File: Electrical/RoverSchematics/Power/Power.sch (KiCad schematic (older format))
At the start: 4 parts

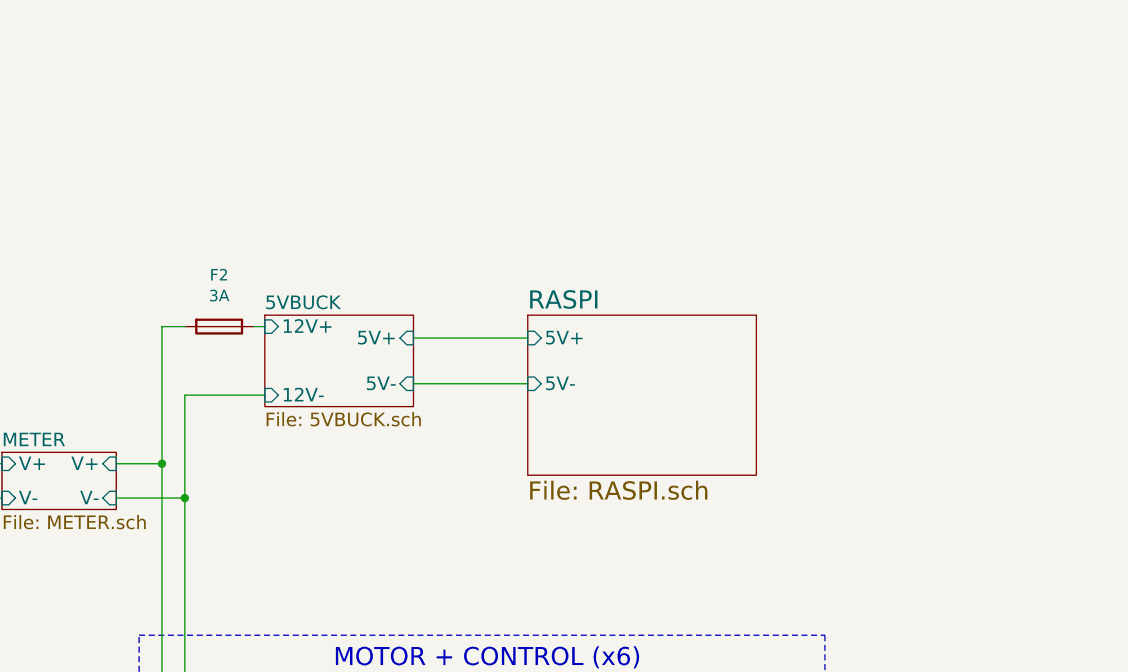
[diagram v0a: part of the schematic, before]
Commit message: Added PWM HAT and Servos to Block Diagram
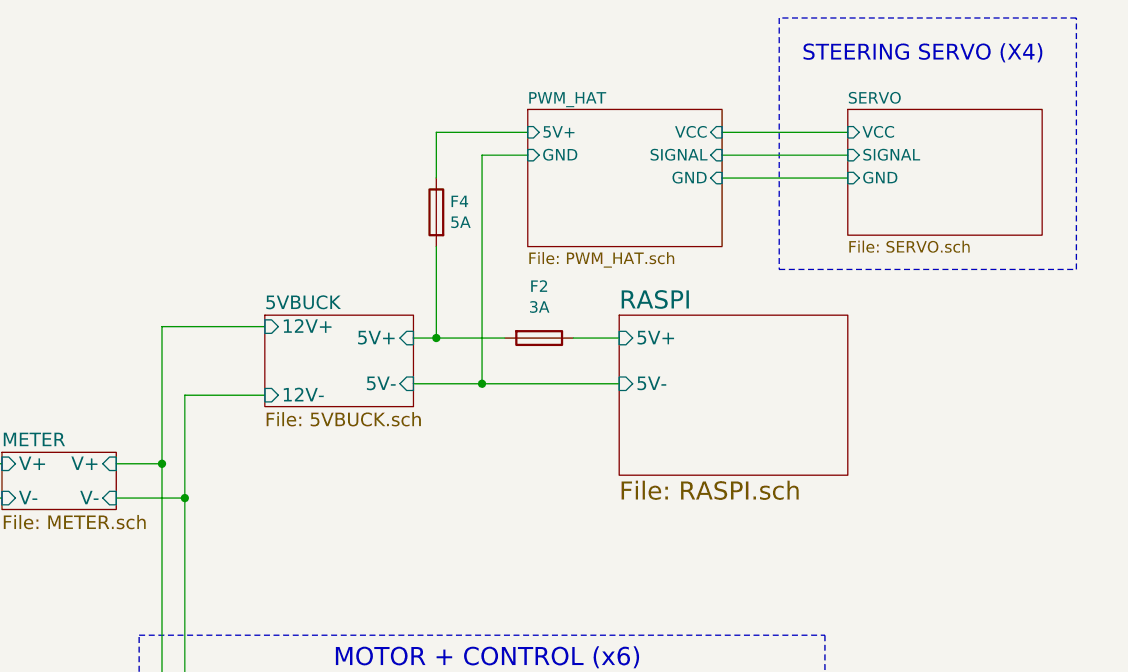
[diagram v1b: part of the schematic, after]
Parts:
- added F4: 5A, symbol Device:Fuse
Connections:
- net 5VBUCK/12V+: now also F3.2; no longer F2.1
- net 5VBUCK/5V+: now also F2.2, F4.2
- removed net METER/V+: F2.2, F3.2
- new net PWM_HAT/5V+: F4.1
- new net RASPI/5V+: F2.1
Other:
- note added: "STEERING SERVO (X4)"
- moved on the sheet: F2
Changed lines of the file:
@@
 EESchema Schematic File Version 4
+LIBS:Power-cache
 EELAYER 26 0
 EELAYER END
 $Descr A4 11693 8268
 encoding utf-8
-Sheet 1 8
+Sheet 1 10
 Title "MINIROVER POWER DIAGRAM"
 Date "2018-10-21"
@@
 L Device:Fuse F2
 U 1 1 5BD0A919
-P 5950 2550
-F 0 "F2" V 5725 2550 50  0000 C CNN
-F 1 "3A" V 5816 2550 50  0000 C CNN
-F 2 "" H 6000 2350 50  0001 L CNN
-F 3 "~" H 5950 2550 50  0001 C CNN
-	1    5950 2550
+P 7350 2600
+F 0 "F2" V 7125 2600 50  0000 C CNN
+F 1 "3A" V 7216 2600 50  0000 C CNN
+F 2 "" H 7400 2400 50  0001 L CNN
+F 3 "~" H 7350 2600 50  0001 C CNN
+	1    7350 2600
 	0    1    1    0
 $EndComp
-Wire Wire Line
-	5700 2550 5800 2550
-Wire Wire Line
-	6100 2550 6150 2550
 Wire Wire Line
 	5800 2850 6150 2850
@@
 	5800 4600 6300 4600
 $Sheet
-S 7300 2500 1000 700
+S 7700 2500 1000 700
 U 5BD0F6A9
 F0 "RASPI" 79
 F1 "RASPI.sch" 79
-F2 "5V+" I L 7300 2600 59
-F3 "5V-" I L 7300 2800 59
-$EndSheet
-Wire Wire Line
-	7300 2600 6800 2600
-Wire Wire Line
-	7300 2800 6800 2800
+F2 "5V+" I L 7700 2600 59
+F3 "5V-" I L 7700 2800 59
+$EndSheet
+$Sheet
+S 7300 1600 850  600
+U 5BDB4C8F
+F0 "PWM_HAT" 50
+F1 "PWM_HAT.sch" 50
+F2 "5V+" I L 7300 1700 50
+F3 "GND" I L 7300 1800 50
+F4 "VCC" I R 8150 1700 50
+F5 "SIGNAL" I R 8150 1800 50
+F6 "GND" I R 8150 1900 50
+$EndSheet
+Wire Wire Line
+	7300 1800 7100 1800
+Wire Wire Line
+	7100 1800 7100 2800
+Wire Wire Line
+	7100 2800 6800 2800
+$Sheet
+S 8700 1600 850  550
+U 5BDB5877
+F0 "SERVO" 50
+F1 "SERVO.sch" 50
+F2 "VCC" I L 8700 1700 50
+F3 "SIGNAL" I L 8700 1800 50
+F4 "GND" I L 8700 1900 50
+$EndSheet
+Wire Wire Line
+	8150 1700 8700 1700
+Wire Wire Line
+	8150 1800 8700 1800
+Wire Wire Line
+	8700 1900 8150 1900
+Wire Notes Line
+	8400 1200 8400 2300
+Wire Notes Line
+	8400 2300 9700 2300
+Wire Notes Line
+	9700 2300 9700 1200
+Wire Notes Line
+	9700 1200 8400 1200
+Text Notes 8500 1400 0    69   ~ 0
+STEERING SERVO (X4)
+Wire Wire Line
+	7100 2800 7700 2800
+Connection ~ 7100 2800
+Wire Wire Line
+	5700 2550 6150 2550
+Wire Wire Line
+	7500 2600 7700 2600
+Wire Wire Line
+	6800 2600 6900 2600
+$Comp
+L Device:Fuse F4
+U 1 1 5BDBADD3
+P 6900 2050
+F 0 "F4" H 6840 2096 50  0000 R CNN
+F 1 "5A" H 6840 2005 50  0000 R CNN
+F 2 "" V 6830 2050 50  0001 C CNN
+F 3 "~" H 6900 2050 50  0001 C CNN
+	1    6900 2050
+	-1   0    0    -1
+$EndComp
+Wire Wire Line
+	6900 1900 6900 1700
+Wire Wire Line
+	6900 2200 6900 2600
+Connection ~ 6900 2600
+Wire Wire Line
+	6900 2600 7200 2600
+Wire Wire Line
+	6900 1700 7300 1700
 $EndSCHEMATC

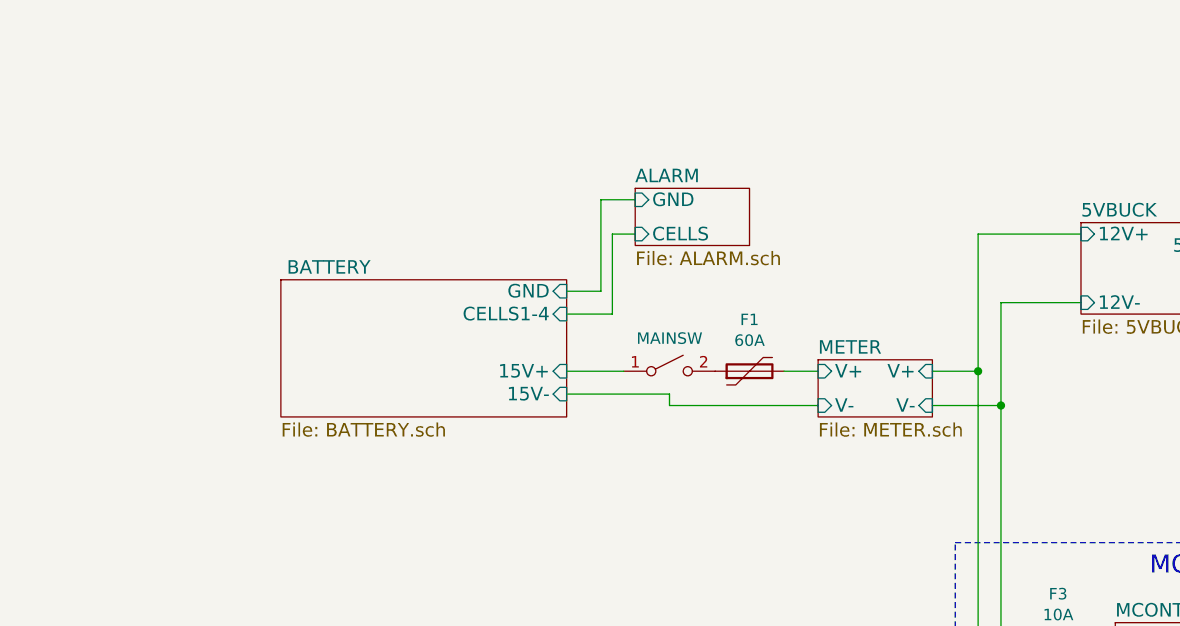
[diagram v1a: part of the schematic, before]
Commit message: Actually fixed drivetrain this time, various small changes
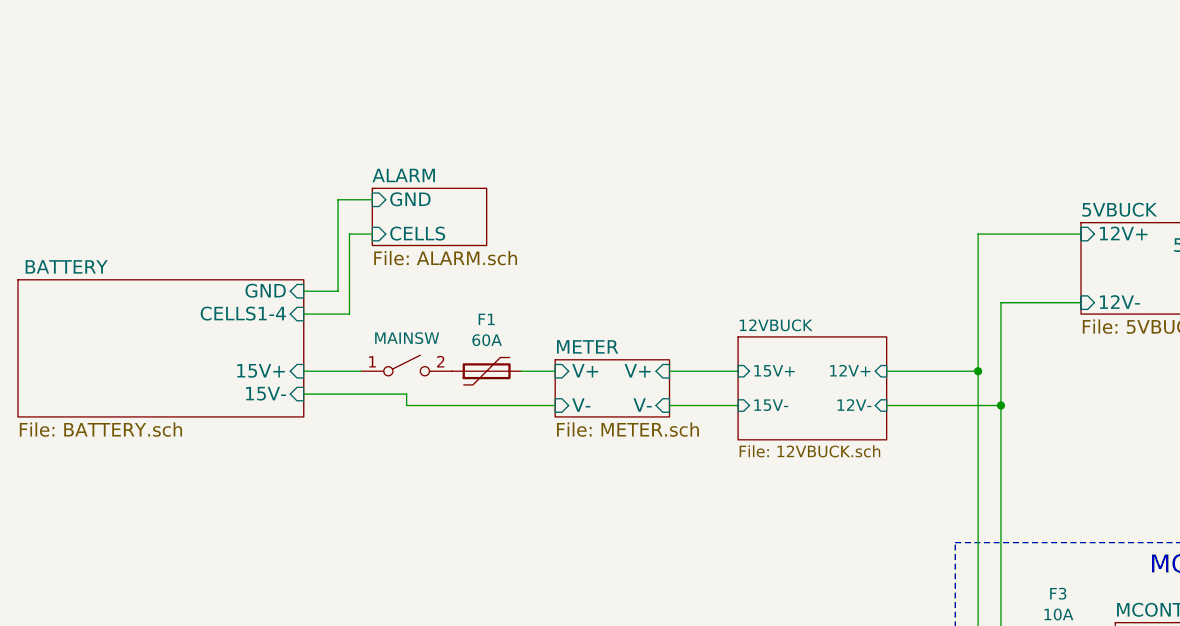
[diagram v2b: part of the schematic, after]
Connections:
- net 5VBUCK/12V+ renamed 12VBUCK/12V+
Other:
- moved on the sheet: F1, MAINSW
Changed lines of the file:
@@
 EESchema Schematic File Version 4
 LIBS:Power-cache
-EELAYER 26 0
+EELAYER 29 0
 EELAYER END
 $Descr A4 11693 8268
@@
 $EndDescr
 $Sheet
-S 2650 2750 1250 600
+S 1500 2750 1250 600
 U 5BCF739B
 F0 " BATTERY" 59
 F1 "BATTERY.sch" 59
-F2 "15V-" I R 3900 3250 59
-F3 "15V+" I R 3900 3150 59
-F4 "GND" I R 3900 2800 59
-F5 "CELLS1-4" I R 3900 2900 59
-$EndSheet
-$Sheet
-S 4200 2350 500  250
+F2 "15V-" I R 2750 3250 59
+F3 "15V+" I R 2750 3150 59
+F4 "GND" I R 2750 2800 59
+F5 "CELLS1-4" I R 2750 2900 59
+$EndSheet
+$Sheet
+S 3050 2350 500  250
 U 5BCF74BF
 F0 "ALARM" 59
 F1 "ALARM.sch" 59
-F2 "GND" I L 4200 2400 59
-F3 "CELLS" I L 4200 2550 59
-$EndSheet
-Wire Wire Line
-	3900 2800 4050 2800
-Wire Wire Line
-	4050 2800 4050 2400
-Wire Wire Line
-	4050 2400 4200 2400
-Wire Wire Line
-	4200 2550 4100 2550
-Wire Wire Line
-	4100 2550 4100 2900
-Wire Wire Line
-	4100 2900 3900 2900
+F2 "GND" I L 3050 2400 59
+F3 "CELLS" I L 3050 2550 59
+$EndSheet
+Wire Wire Line
+	2750 2800 2900 2800
+Wire Wire Line
+	2900 2800 2900 2400
+Wire Wire Line
+	2900 2400 3050 2400
+Wire Wire Line
+	3050 2550 2950 2550
+Wire Wire Line
+	2950 2550 2950 2900
+Wire Wire Line
+	2950 2900 2750 2900
 $Comp
 L Switch:SW_SPST MAINSW
 U 1 1 5BD05F5D
-P 4350 3150
-F 0 "MAINSW" H 4350 3293 50  0000 C CNN
-F 1 "SW_SPST" H 4350 3294 50  0001 C CNN
-F 2 "" H 4350 3150 50  0001 C CNN
-F 3 "" H 4350 3150 50  0001 C CNN
-	1    4350 3150
+P 3200 3150
+F 0 "MAINSW" H 3200 3293 50  0000 C CNN
+F 1 "SW_SPST" H 3200 3294 50  0001 C CNN
+F 2 "" H 3200 3150 50  0001 C CNN
+F 3 "" H 3200 3150 50  0001 C CNN
+	1    3200 3150
 	1    0    0    -1
 $EndComp
 Wire Wire Line
-	3900 3150 4150 3150
-Wire Wire Line
-	4850 3150 5000 3150
-Wire Wire Line
-	4350 3300 4350 3250
-Wire Wire Line
-	4350 3250 3900 3250
+	2750 3150 3000 3150
+Wire Wire Line
+	3700 3150 3850 3150
+Wire Wire Line
+	3200 3300 3200 3250
+Wire Wire Line
+	3200 3250 2750 3250
 $Comp
 L Device:Polyfuse F1
 U 1 1 5BD061FD
-P 4700 3150
-F 0 "F1" V 4925 3150 50  0000 C CNN
-F 1 "60A" V 4834 3150 50  0000 C CNN
-F 2 "" H 4750 2950 50  0001 L CNN
-F 3 "~" H 4700 3150 50  0001 C CNN
-	1    4700 3150
+P 3550 3150
+F 0 "F1" V 3775 3150 50  0000 C CNN
+F 1 "60A" V 3684 3150 50  0000 C CNN
+F 2 "" H 3600 2950 50  0001 L CNN
+F 3 "~" H 3550 3150 50  0001 C CNN
+	1    3550 3150
 	0    -1   -1   0
 $EndComp
 Wire Wire Line
-	4350 3300 5000 3300
+	3200 3300 3850 3300
 $Sheet
 S 6150 2500 650  400
@@
 $EndSheet
 $Sheet
-S 5000 3100 500  250
+S 3850 3100 500  250
 U 5BD05FEE
 F0 "METER" 59
 F1 "METER.sch" 59
-F2 "V+" I L 5000 3150 59
-F3 "V-" I L 5000 3300 59
-F4 "V+" I R 5500 3150 59
-F5 "V-" I R 5500 3300 59
-$EndSheet
-Wire Wire Line
-	5500 3150 5700 3150
-Wire Wire Line
-	5500 3300 5800 3300
+F2 "V+" I L 3850 3150 59
+F3 "V-" I L 3850 3300 59
+F4 "V+" I R 4350 3150 59
+F5 "V-" I R 4350 3300 59
+$EndSheet
 Wire Wire Line
 	5700 3150 5700 2550
@@
 Wire Wire Line
 	6900 1700 7300 1700
+$Sheet
+S 4650 3000 650  450
+U 5CABF463
+F0 "12VBUCK" 50
+F1 "12VBUCK.sch" 50
+F2 "15V-" I L 4650 3300 50
+F3 "15V+" I L 4650 3150 50
+F4 "12V+" I R 5300 3150 50
+F5 "12V-" I R 5300 3300 50
+$EndSheet
+Wire Wire Line
+	5300 3150 5700 3150
+Wire Wire Line
+	5300 3300 5800 3300
+Wire Wire Line
+	4650 3150 4350 3150
+Wire Wire Line
+	4350 3300 4650 3300
 $EndSCHEMATC
